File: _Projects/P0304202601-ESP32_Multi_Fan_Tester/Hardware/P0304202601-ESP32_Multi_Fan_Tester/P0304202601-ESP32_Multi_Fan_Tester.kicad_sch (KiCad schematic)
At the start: 3 parts

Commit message: Added updated content that I keep forgetting to do.
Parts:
- added FID4, FID5, FID6: ~, COMPONENTS:FID1.0x1.5mm Round, symbol COMPONENTS:FID1.0x1.5mmROUND
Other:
- moved on the sheet: FID1, FID2, FID3
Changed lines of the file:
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@@
 	(symbol
 		(lib_id "COMPONENTS:FID1.0x1.5mmROUND")
-		(at 215.9 152.4 0)
+		(at 241.3 139.7 0)
 		(unit 1)
 		(exclude_from_sim no)
@@
 		(fields_autoplaced yes)
 		(property "Reference" "FID1"
-			(at 218.44 151.1299 0)
-			(effects
-				(font
-					(size 1.27 1.27)
-				)
-				(justify left)
-			)
-		)
-		(property "Value" "~"
-			(at 218.44 153.6699 0)
-			(effects
-				(font
-					(size 1.27 1.27)
-				)
-				(justify left)
-			)
-		)
-		(property "Footprint" "COMPONENTS:FID1.0x1.5mm Round"
-			(at 215.9 152.4 0)
-			(effects
-				(font
-					(size 1.27 1.27)
-				)
-				(hide yes)
-			)
-		)
-		(property "Datasheet" ""
-			(at 215.9 152.4 0)
-			(effects
-				(font
-					(size 1.27 1.27)
-				)
-				(hide yes)
-			)
-		)
-		(property "Description" ""
-			(at 215.9 152.4 0)
+			(at 243.84 138.4299 0)
+			(effects
+				(font
+					(size 1.27 1.27)
+				)
+				(justify left)
+			)
+		)
+		(property "Value" "~"
+			(at 243.84 140.9699 0)
+			(effects
+				(font
+					(size 1.27 1.27)
+				)
+				(justify left)
+			)
+		)
+		(property "Footprint" "COMPONENTS:FID1.0x1.5mm Round"
+			(at 241.3 139.7 0)
+			(effects
+				(font
+					(size 1.27 1.27)
+				)
+				(hide yes)
+			)
+		)
+		(property "Datasheet" ""
+			(at 241.3 139.7 0)
+			(effects
+				(font
+					(size 1.27 1.27)
+				)
+				(hide yes)
+			)
+		)
+		(property "Description" ""
+			(at 241.3 139.7 0)
 			(effects
 				(font
@@
 	(symbol
 		(lib_id "COMPONENTS:FID1.0x1.5mmROUND")
-		(at 228.6 152.4 0)
+		(at 254 148.59 0)
+		(unit 1)
+		(exclude_from_sim no)
+		(in_bom no)
+		(on_board yes)
+		(dnp no)
+		(fields_autoplaced yes)
+		(property "Reference" "FID5"
+			(at 256.54 147.3199 0)
+			(effects
+				(font
+					(size 1.27 1.27)
+				)
+				(justify left)
+			)
+		)
+		(property "Value" "~"
+			(at 256.54 149.8599 0)
+			(effects
+				(font
+					(size 1.27 1.27)
+				)
+				(justify left)
+			)
+		)
+		(property "Footprint" "COMPONENTS:FID1.0x1.5mm Round"
+			(at 254 148.59 0)
+			(effects
+				(font
+					(size 1.27 1.27)
+				)
+				(hide yes)
+			)
+		)
+		(property "Datasheet" ""
+			(at 254 148.59 0)
+			(effects
+				(font
+					(size 1.27 1.27)
+				)
+				(hide yes)
+			)
+		)
+		(property "Description" ""
+			(at 254 148.59 0)
+			(effects
+				(font
+					(size 1.27 1.27)
+				)
+				(hide yes)
+			)
+		)
+		(pin "1"
+		)
+		(instances
+			(project "P0304202601-ESP32_Multi_Fan_Tester"
+				(path "/da4b17a0-c783-4eac-be85-8eec7b7dd8dd"
+					(reference "FID5")
+					(unit 1)
+				)
+			)
+		)
+	)
+	(symbol
+		(lib_id "COMPONENTS:FID1.0x1.5mmROUND")
+		(at 266.7 148.59 0)
+		(unit 1)
+		(exclude_from_sim no)
+		(in_bom no)
+		(on_board yes)
+		(dnp no)
+		(fields_autoplaced yes)
+		(property "Reference" "FID6"
+			(at 269.24 147.3199 0)
+			(effects
+				(font
+					(size 1.27 1.27)
+				)
+				(justify left)
+			)
+		)
+		(property "Value" "~"
+			(at 269.24 149.8599 0)
+			(effects
+				(font
+					(size 1.27 1.27)
+				)
+				(justify left)
+			)
+		)
+		(property "Footprint" "COMPONENTS:FID1.0x1.5mm Round"
+			(at 266.7 148.59 0)
+			(effects
+				(font
+					(size 1.27 1.27)
+				)
+				(hide yes)
+			)
+		)
+		(property "Datasheet" ""
+			(at 266.7 148.59 0)
+			(effects
+				(font
+					(size 1.27 1.27)
+				)
+				(hide yes)
+			)
+		)
+		(property "Description" ""
+			(at 266.7 148.59 0)
+			(effects
+				(font
+					(size 1.27 1.27)
+				)
+				(hide yes)
+			)
+		)
+		(pin "1"
+		)
+		(instances
+			(project "P0304202601-ESP32_Multi_Fan_Tester"
+				(path "/da4b17a0-c783-4eac-be85-8eec7b7dd8dd"
+					(reference "FID6")
+					(unit 1)
+				)
+			)
+		)
+	)
+	(symbol
+		(lib_id "COMPONENTS:FID1.0x1.5mmROUND")
+		(at 254 139.7 0)
 		(unit 1)
 		(exclude_from_sim no)
@@
 		(fields_autoplaced yes)
 		(property "Reference" "FID2"
-			(at 231.14 151.1299 0)
-			(effects
-				(font
-					(size 1.27 1.27)
-				)
-				(justify left)
-			)
-		)
-		(property "Value" "~"
-			(at 231.14 153.6699 0)
-			(effects
-				(font
-					(size 1.27 1.27)
-				)
-				(justify left)
-			)
-		)
-		(property "Footprint" "COMPONENTS:FID1.0x1.5mm Round"
-			(at 228.6 152.4 0)
-			(effects
-				(font
-					(size 1.27 1.27)
-				)
-				(hide yes)
-			)
-		)
-		(property "Datasheet" ""
-			(at 228.6 152.4 0)
-			(effects
-				(font
-					(size 1.27 1.27)
-				)
-				(hide yes)
-			)
-		)
-		(property "Description" ""
-			(at 228.6 152.4 0)
+			(at 256.54 138.4299 0)
+			(effects
+				(font
+					(size 1.27 1.27)
+				)
+				(justify left)
+			)
+		)
+		(property "Value" "~"
+			(at 256.54 140.9699 0)
+			(effects
+				(font
+					(size 1.27 1.27)
+				)
+				(justify left)
+			)
+		)
+		(property "Footprint" "COMPONENTS:FID1.0x1.5mm Round"
+			(at 254 139.7 0)
+			(effects
+				(font
+					(size 1.27 1.27)
+				)
+				(hide yes)
+			)
+		)
+		(property "Datasheet" ""
+			(at 254 139.7 0)
+			(effects
+				(font
+					(size 1.27 1.27)
+				)
+				(hide yes)
+			)
+		)
+		(property "Description" ""
+			(at 254 139.7 0)
 			(effects
 				(font
@@
 	(symbol
 		(lib_id "COMPONENTS:FID1.0x1.5mmROUND")
-		(at 241.3 152.4 0)
+		(at 241.3 148.59 0)
+		(unit 1)
+		(exclude_from_sim no)
+		(in_bom no)
+		(on_board yes)
+		(dnp no)
+		(fields_autoplaced yes)
+		(property "Reference" "FID4"
+			(at 243.84 147.3199 0)
+			(effects
+				(font
+					(size 1.27 1.27)
+				)
+				(justify left)
+			)
+		)
+		(property "Value" "~"
+			(at 243.84 149.8599 0)
+			(effects
+				(font
+					(size 1.27 1.27)
+				)
+				(justify left)
+			)
+		)
+		(property "Footprint" "COMPONENTS:FID1.0x1.5mm Round"
+			(at 241.3 148.59 0)
+			(effects
+				(font
+					(size 1.27 1.27)
+				)
+				(hide yes)
+			)
+		)
+		(property "Datasheet" ""
+			(at 241.3 148.59 0)
+			(effects
+				(font
+					(size 1.27 1.27)
+				)
+				(hide yes)
+			)
+		)
+		(property "Description" ""
+			(at 241.3 148.59 0)
+			(effects
+				(font
+					(size 1.27 1.27)
+				)
+				(hide yes)
+			)
+		)
+		(pin "1"
+		)
+		(instances
+			(project "P0304202601-ESP32_Multi_Fan_Tester"
+				(path "/da4b17a0-c783-4eac-be85-8eec7b7dd8dd"
+					(reference "FID4")
+					(unit 1)
+				)
+			)
+		)
+	)
+	(symbol
+		(lib_id "COMPONENTS:FID1.0x1.5mmROUND")
+		(at 266.7 139.7 0)
 		(unit 1)
 		(exclude_from_sim no)
@@
 		(fields_autoplaced yes)
 		(property "Reference" "FID3"
-			(at 243.84 151.1299 0)
-			(effects
-				(font
-					(size 1.27 1.27)
-				)
-				(justify left)
-			)
-		)
-		(property "Value" "~"
-			(at 243.84 153.6699 0)
-			(effects
-				(font
-					(size 1.27 1.27)
-				)
-				(justify left)
-			)
-		)
-		(property "Footprint" "COMPONENTS:FID1.0x1.5mm Round"
-			(at 241.3 152.4 0)
-			(effects
-				(font
-					(size 1.27 1.27)
-				)
-				(hide yes)
-			)
-		)
-		(property "Datasheet" ""
-			(at 241.3 152.4 0)
-			(effects
-				(font
-					(size 1.27 1.27)
-				)
-				(hide yes)
-			)
-		)
-		(property "Description" ""
-			(at 241.3 152.4 0)
-			(effects
-				(font
+			(at 269.24 138.4299 0)
+			(effects
+				(font
+					(size 1.27 1.27)
+				)
+				(justify left)
+			)
+		)
+		(property "Value" "~"
+			(at 269.24 140.9699 0)
+			(effects
+				(font
+					(size 1.27 1.27)
+				)
+				(justify left)
+			)
+		)
+		(property "Footprint" "COMPONENTS:FID1.0x1.5mm Round"
+			(at 266.7 139.7 0)
+			(effects
+				(font
+					(size 1.27 1.27)
+				)
+				(hide yes)
+			)
+		)
+		(property "Datasheet" ""
+			(at 266.7 139.7 0)
+			(effects
+				(font
+					(size 1.27 1.27)
+				)
+				(hide yes)
+			)
+		)
+		(property "Description" ""
+			(at 266.7 139.7 0)
+			(effects
+				(font

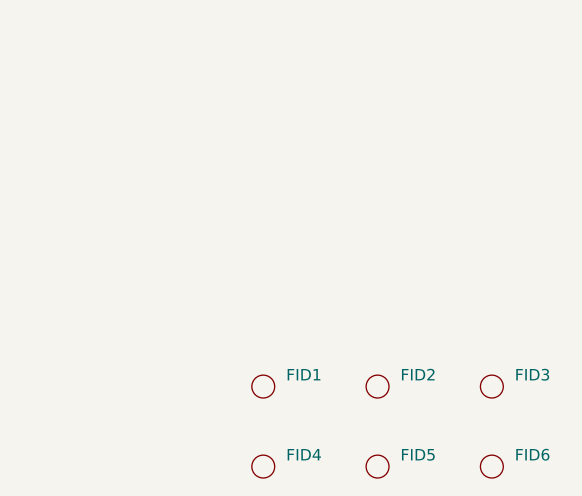
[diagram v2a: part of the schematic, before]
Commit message: Updated files from video stream.
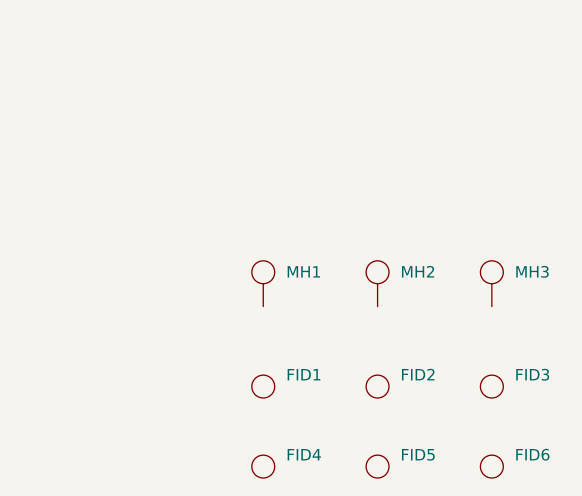
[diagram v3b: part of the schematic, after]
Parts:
- added MH1, MH2, MH3: (no value), HARDWARE:M3MountingHole, symbol HARDWARE:M3MountingHole
- FID1, FID2, FID3, FID4, FID5, FID6: value ~ -> (none)
